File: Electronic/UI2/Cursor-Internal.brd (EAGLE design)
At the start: 160 x 100 mm, 7 parts

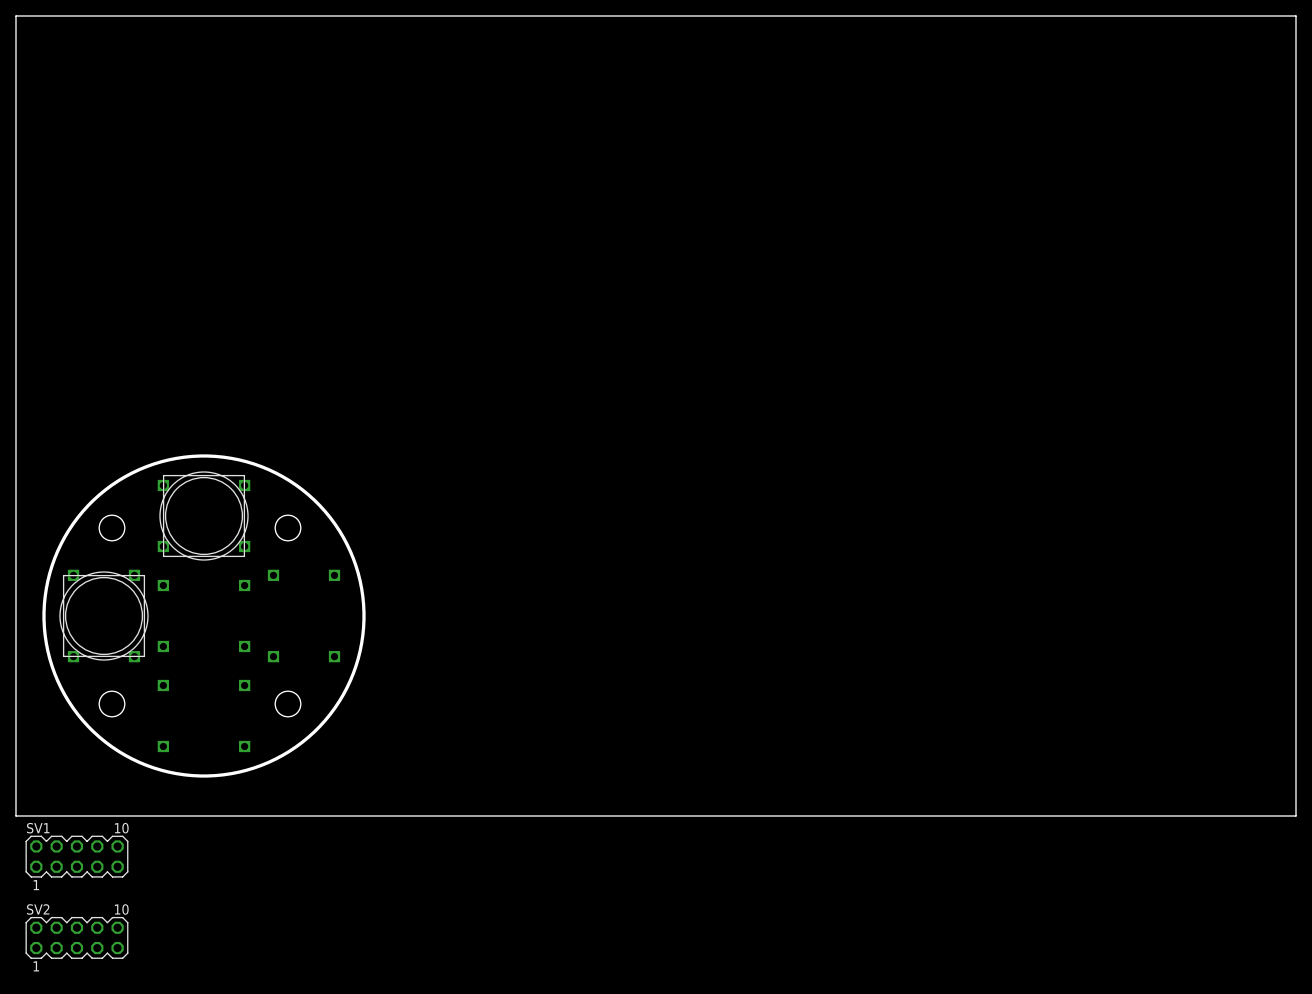
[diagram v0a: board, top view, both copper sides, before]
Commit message: adding a new CursorCross for EC60A/B usage
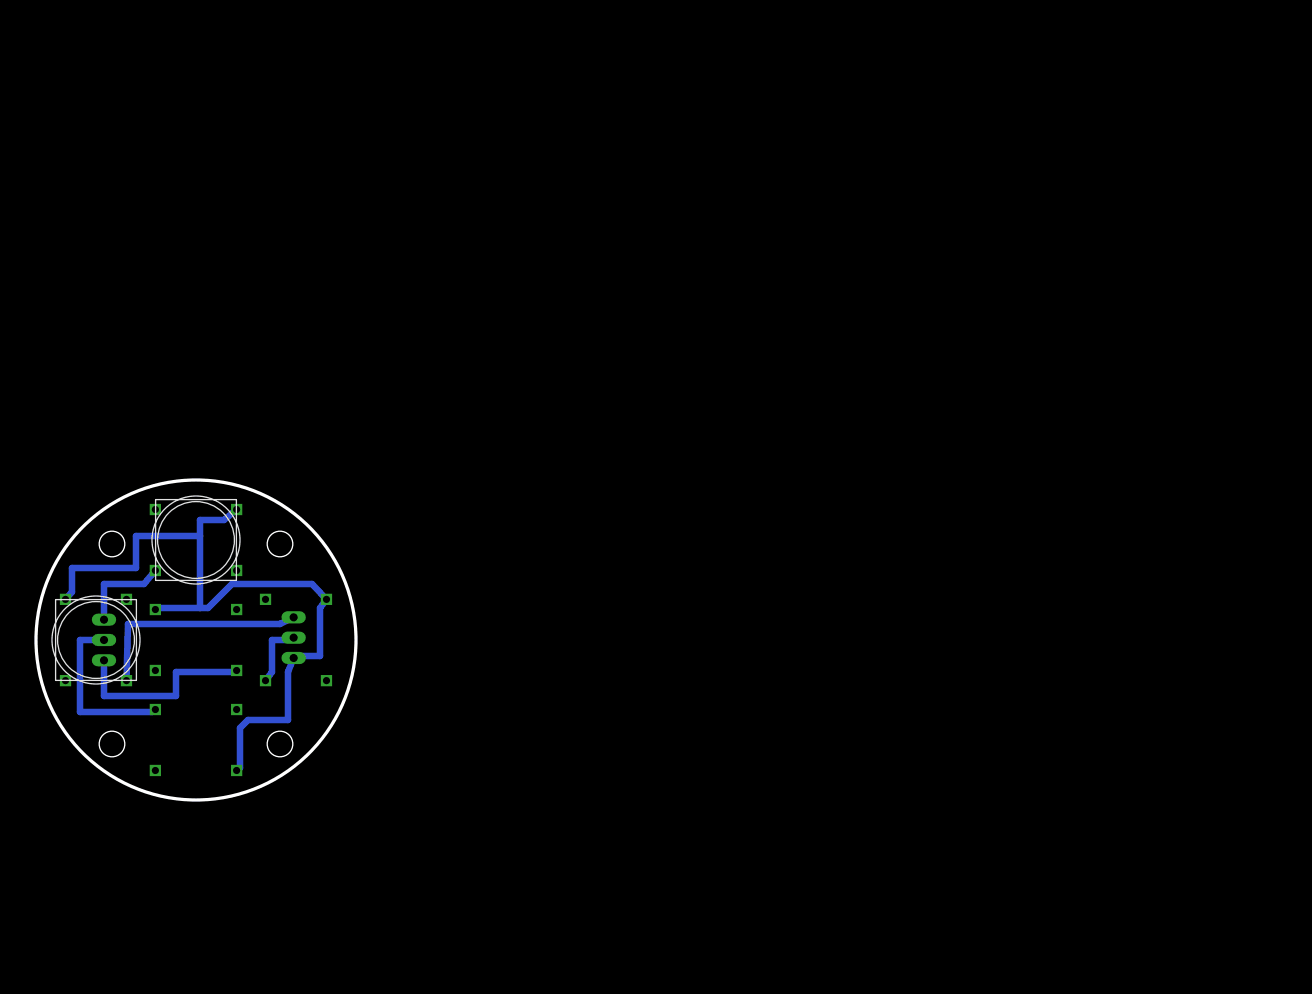
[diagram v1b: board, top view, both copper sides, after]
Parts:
- removed SV1: Debounce L, con-lstb:MA05-2
- removed SV2: Debounce R, con-lstb:MA05-2
- added JP1, JP2: (no value), pinhead:1X03
- moved KEY_CENTER 3.16 mm to (22.5, 22.0)
- moved KEY_DOWN 3.16 mm to (22.5, 9.50), turned to 0 degrees
- moved KEY_LEFT 3.16 mm to (10.0, 22.0)
- moved KEY_RIGHT 3.16 mm to (35.0, 22.0)
- moved KEY_UP 3.16 mm to (22.5, 34.5)
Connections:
- removed net N$6: SV2.10, SV2.9
- removed net N$7: SV2.7, SV2.8
- removed net N$8: SV2.5, SV2.6
- removed net N$9: SV2.3, SV2.4
- net GND: now also JP1.3; no longer KEY_CENTER.P$3, KEY_DOWN.P$3, KEY_LEFT.P$3, KEY_RIGHT.P$3, KEY_UP.P$3, SV2.1, SV2.2
- net KEY_CENTER: now also JP2.1; no longer KEY_CENTER.P$2, SV1.10, SV1.9
- net KEY_DOWN: now also JP2.2; no longer KEY_DOWN.P$2, SV1.7, SV1.8
- net KEY_LEFT: now also JP1.1; no longer KEY_LEFT.P$2, SV1.3, SV1.4
- net KEY_RIGHT: now also JP1.2; no longer KEY_RIGHT.P$2, SV1.1, SV1.2
- net KEY_UP: now also JP2.3; no longer KEY_UP.P$2, SV1.5, SV1.6
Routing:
- net GND: track 0.00 -> 94.3 mm
- net KEY_LEFT: track 0.00 -> 28.0 mm
- net KEY_CENTER: track 0.00 -> 24.1 mm
- net KEY_DOWN: track 0.00 -> 21.5 mm
- net KEY_UP: track 0.00 -> 11.7 mm
- net KEY_RIGHT: track 0.00 -> 8.12 mm
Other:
- board size 160 x 100 mm -> 40 x 40 mm
